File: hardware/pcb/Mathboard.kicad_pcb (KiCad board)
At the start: 2 copper layers, 95.6 x 74.3 mm, 44 parts, among them J1 TSW-112-06-T-S, J2 TSW-112-06-T-S, J4 Conn_01x07_Pin, SW1 SW_Push, SW10 SW_Push, SW11 SW_Push, SW12 SW_Push, SW13 SW_Push, SW14 SW_Push, SW15 SW_Push, SW16 SW_Push, SW17 PCM13SMTR, SW2 SW_Push, SW3 SW_Push, SW4 SW_Push, SW5 SW_Push, SW6 SW_Push, SW7 SW_Push, SW8 SW_Push, SW9 SW_Push

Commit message: Progress towards version 2
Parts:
- removed J1, J2: TSW-112-06-T-S, Connector_PinHeader_2.54mm:PinHeader_1x12_P2.54mm_Vertical
- removed J4: Conn_01x07_Pin, Connector_PinHeader_2.54mm:PinHeader_1x07_P2.54mm_Vertical
- removed REF**: OSHW-Logo_7.5x8mm_SilkScreen, Symbol:OSHW-Logo_7.5x8mm_SilkScreen
- removed REF**: KiCad-Logo_5mm_SilkScreen, Symbol:KiCad-Logo_5mm_SilkScreen
- removed REF**: WEEE-Logo_5.6x8mm_SilkScreen, Symbol:WEEE-Logo_5.6x8mm_SilkScreen
- added C10: 1u, Capacitor_SMD:C_0402_1005Metric, B.Cu at (100.5, 107.2)
- added C11: 1u, Capacitor_SMD:C_0402_1005Metric, B.Cu at (100.5, 106.0)
- added C12: 100n, Capacitor_SMD:C_0402_1005Metric, B.Cu at (110.8, 107.2)
- added C13: 100n, Capacitor_SMD:C_0402_1005Metric, B.Cu at (106.6, 101.8)
- added C14: 100n, Capacitor_SMD:C_0402_1005Metric, B.Cu at (100.5, 109.4)
- added C15: 100n, Capacitor_SMD:C_0402_1005Metric, B.Cu at (175.6, 47.7)
- added C16: 100n, Capacitor_SMD:C_0402_1005Metric, B.Cu at (102.5, 102.1)
- added C17: 100n, Capacitor_SMD:C_0402_1005Metric, B.Cu at (100.5, 110.3)
- added C18: 100n, Capacitor_SMD:C_0402_1005Metric, B.Cu at (110.6, 108.1)
- added C19: 100n, Capacitor_SMD:C_0402_1005Metric, B.Cu at (106.6, 112.0)
- added C2: 10u, Capacitor_SMD:C_0402_1005Metric, B.Cu at (128.2, 50.8)
- added C20: 100n, Capacitor_SMD:C_0402_1005Metric, B.Cu at (100.5, 108.5)
- added C3: 4.7u, Capacitor_SMD:C_0402_1005Metric, B.Cu at (108.7, 99.9)
- added C4: 10u, Capacitor_SMD:C_0402_1005Metric, B.Cu at (109.6, 99.9)
- added C5: 10u, Capacitor_SMD:C_0402_1005Metric, B.Cu at (124.1, 57.8)
- added C6: 10u, Capacitor_SMD:C_0402_1005Metric, B.Cu at (120.8, 55.2)
- added C7: 100n, Capacitor_SMD:C_0402_1005Metric, B.Cu at (93.4, 112.1)
- added C8: 15p, Capacitor_SMD:C_0402_1005Metric, B.Cu at (110.7, 105.0)
- added C9: 15p, Capacitor_SMD:C_0402_1005Metric, B.Cu at (115.0, 105.0)
- added D17: PMEG2010BELD, Diode_SMD:D_SOD-882D, B.Cu at (126.3, 54.2)
- added F1: 500mA, Fuse:Fuse_0603_1608Metric, B.Cu at (127.7, 52.8)
- added FB1: 600R, Resistor_SMD:R_0402_1005Metric, B.Cu at (129.6, 50.9)
- added J3: GT-USB-7010ASV, mathboard:USB_C_Receptacle_G-Switch_GT-USB-7010ASV, B.Cu at (124.7, 45.1)
- added Q1: 2N7002VC-, Package_TO_SOT_SMD:SOT-563, B.Cu at (116.7, 101.6)
- added Q2: 2N7002VC-, Package_TO_SOT_SMD:SOT-563, B.Cu at (104.8, 99.9)
- added R1: 10k, Resistor_SMD:R_0402_1005Metric, B.Cu at (117.6, 107.1)
- added R11: 10k, Resistor_SMD:R_0402_1005Metric, B.Cu at (93.4, 101.5)
- added R12: 27, Resistor_SMD:R_0402_1005Metric, B.Cu at (101.5, 112.0)
- added R13: 27, Resistor_SMD:R_0402_1005Metric, B.Cu at (102.5, 112.0)
- added R14: 1k, Resistor_SMD:R_0402_1005Metric, B.Cu at (113.2, 107.0)
- added R2: 10k, Resistor_SMD:R_0402_1005Metric, B.Cu at (102.4, 100.4)
- added R3: 10k, Resistor_SMD:R_0402_1005Metric, B.Cu at (116.7, 107.1)
- added R4: 51k, Resistor_SMD:R_0402_1005Metric, B.Cu at (106.7, 99.9)
- added R5: 51k, Resistor_SMD:R_0402_1005Metric, B.Cu at (107.7, 99.9)
- added R6: 51k, Resistor_SMD:R_0402_1005Metric, B.Cu at (108.2, 101.4)
- added R7: 5.1k, Resistor_SMD:R_0402_1005Metric, B.Cu at (121.9, 50.5)
- added R8: 5.1k, Resistor_SMD:R_0402_1005Metric, B.Cu at (126.3, 51.0)
- added R9: 1k, Resistor_SMD:R_0402_1005Metric, B.Cu at (99.4, 99.8)
- added SW18: SWITCH, mathboard:SW_Push_1P1T_XKB_TS-1187A, B.Cu at (121.0, 104.3)
- added U3: USBLC6-2P6, Package_TO_SOT_SMD:SOT-666, B.Cu at (121.3, 52.4)
- added U4: TLV74333PDBVR, Package_TO_SOT_SMD:SOT-23-5, B.Cu at (123.4, 55.7)
- added U5: W25Q128JVPIQ, Package_SO:SOIC-8W_5.3x5.3mm_P1.27mm, B.Cu at (95.8, 106.8)
- added U6: RP2040, Package_DFN_QFN:QFN-56-1EP_7x7mm_P0.4mm_EP3.2x3.2mm, B.Cu at (105.6, 106.8)
- added U7: 74LVC1T45, Package_TO_SOT_SMD:SOT-563, B.Cu at (175.3, 45.8)
- added Y1: 12MHz, Crystal:Crystal_SMD_2520-4Pin_2.5x2.0mm, B.Cu at (112.9, 105.0)
- moved U2 99.9 mm to (170.5, 45.8), turned to 0 degrees
- moved C1 93.5 mm to (166.2, 45.8), turned to -90 degrees
- moved D4 13.8 mm to (147.5, 51.4)
- moved D16 13.5 mm to (157.8, 105.5), turned to -90 degrees
- moved D15 13.4 mm to (129.2, 105.5), turned to -90 degrees
- moved D3 9.67 mm to (137.7, 51.4)
- moved SW17 9.40 mm to (139.7, 45.4)
- moved D5 6.58 mm to (167.0, 51.4), turned to -90 degrees
- moved H3 2.90 mm to (116.9, 112.3)
- moved D10 2.80 mm to (89.5, 83.5)
- moved D11 1.11 mm to (107.2, 86.5)
- moved D12 1.11 mm to (126.2, 86.5)
- moved D6 1.11 mm to (99.2, 67.5)
- moved D7 1.11 mm to (118.2, 67.5)
- moved D13 1.11 mm to (145.2, 86.5)
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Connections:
- net VDD renamed +5V
- SW17 pad 1: Net-(J2-Pin_11) -> /Microcontroller/7
- SW17 pad 2: Net-(J2-Pin_12) -> /Microcontroller/8
- SW17 pad 4: Net-(J4-Pin_1) -> /Microcontroller/9
- U2 pad 4: RGB_DIN -> /RGB_DIN
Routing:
- net GND: track 191.5 -> 39.7 mm, vias 1 -> 26
- net RGB_DIN: track 149.1 -> 0.00 mm, vias 2 -> 0
- net /Microcontroller/RGB_DO: track 0.00 -> 136.7 mm, vias 0 -> 2
- net /Microcontroller/USB-: track 0.00 -> 129.8 mm
- net /Microcontroller/USB+: track 0.00 -> 129.7 mm
- net +5V: track 173.4 -> 54.4 mm, vias 0 -> 2
- net /Microcontroller/9: track 0.00 -> 94.1 mm, vias 0 -> 2
- net /Microcontroller/8: track 0.00 -> 89.2 mm, vias 0 -> 2
- net /Microcontroller/7: track 0.00 -> 88.2 mm, vias 0 -> 2
- net ROW0: track 91.0 -> 147.3 mm, vias 0 -> 7
- net ROW1: track 65.5 -> 107.3 mm, vias 0 -> 6
- net COL2: track 65.0 -> 105.9 mm, vias 0 -> 2
- net COL4: track 95.5 -> 131.2 mm, vias 0 -> 2
- net Net-(J2-Pin_11): track 34.4 -> 0.00 mm
- net Net-(J2-Pin_12): track 30.3 -> 0.00 mm
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- added copper zone on B.Cu, net +3V3
- added copper zone on In1.Cu, net +3V3
- added copper zone on B.Cu, net +5V
- added copper zone on B.Cu, net /Microcontroller/RGB_DO
- added copper zone on B.Cu, net GND
- added copper zone on In2.Cu, net GND
- added copper zone on B.Cu, net Net-(J3-SHIELD)
- added copper zone on B.Cu, net VBUS
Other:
- copper layers 2 -> 4

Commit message: Version 2 sent to production
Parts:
- removed C9: 15p, Capacitor_SMD:C_0402_1005Metric
- removed FB1: 600R, Resistor_SMD:R_0402_1005Metric
- added C21: 4.7u, Capacitor_SMD:C_0402_1005Metric, B.Cu at (124.0, 56.3)
- added D18: A-SP192SGHC-C01-3C, mathboard:LED_SMD_0603_flat, B.Cu at (114.0, 43.2)
- added R10: 27, Resistor_SMD:R_0603_1608Metric, B.Cu at (105.9, 47.2)
- added R15: 27, Resistor_SMD:R_0603_1608Metric, B.Cu at (107.6, 47.2)
- added REF** (x2): OSHW-Logo_11.4x12mm_Copper, Symbol:OSHW-Logo_11.4x12mm_Copper, B.Cu at (148.6, 101.8)
- added REF** (x2): OSHW-Logo2_9.8x8mm_Copper, Symbol:OSHW-Logo2_9.8x8mm_Copper, B.Cu at (148.6, 112.3)
- added RV1: 20k, Potentiometer_SMD:Potentiometer_Bourns_TC33X_Vertical, B.Cu at (102.3, 47.6)
- added TP1: TestPoint, TestPoint:TestPoint_Pad_2.0x2.0mm, B.Cu at (88.2, 46.1)
- added TP2: TestPoint, TestPoint:TestPoint_Pad_2.0x2.0mm, B.Cu at (88.2, 49.1)
- added U1: W25Q64JV, Package_SON:WSON-8-1EP_8x6mm_P1.27mm_EP3.4x4.3mm, B.Cu at (95.8, 106.8)
- C2, C4, C5: value 10u -> 4.7u
- C6: value 10u -> 30p; footprint Capacitor_SMD:C_0402_1005Metric -> Capacitor_SMD:C_0603_1608Metric
- C8: value 15p -> 30p; footprint Capacitor_SMD:C_0402_1005Metric -> Capacitor_SMD:C_0603_1608Metric
- D17: value PMEG2010BELD -> DSL14; footprint Diode_SMD:D_SOD-882D -> Diode_SMD:D_SOD-123
- J3: value GT-USB-7010ASV -> TYPE-C sinking plate; footprint mathboard:USB_C_Receptacle_G-Switch_GT-USB-7010ASV -> mathboard:USB_C_Receptacle_XYECONN TYPE-C-F02C-1BBWC1.6
- R12, R13: footprint Resistor_SMD:R_0402_1005Metric -> Resistor_SMD:R_0603_1608Metric
- SW17: value PCM13SMTR -> MSK13C02; footprint mathboard:SWITCH_3SMTR -> mathboard:SWITCH_MSK13C02
- U2: footprint LED_SMD:SK6812-MINI-E -> mathboard:SK6812-MINI-E
- U4: value TLV74333PDBVR -> XC6206P332MR-G; footprint Package_TO_SOT_SMD:SOT-23-5 -> Package_TO_SOT_SMD:SOT-23
- U5: value W25Q128JVPIQ -> PSSI2021SAY; footprint Package_SO:SOIC-8W_5.3x5.3mm_P1.27mm -> Package_TO_SOT_SMD:SOT-353_SC-70-5
- moved U5 62.9 mm to (110.1, 45.5), turned to 180 degrees
- moved C6 50.1 mm to (115.3, 105.0)
- moved D3 12.9 mm to (128.1, 60.0), turned to 90 degrees
- moved D2 11.8 mm to (109.9, 60.3), turned to 90 degrees
- moved D1 10.6 mm to (93.9, 58.7), turned to 90 degrees
- moved D5 8.80 mm to (166.9, 60.2), turned to 90 degrees
- moved D4 8.71 mm to (147.8, 60.1), turned to 90 degrees
- moved C5 5.34 mm to (119.3, 55.5), turned to -90 degrees
- moved SW17 3.04 mm to (142.6, 44.5)
- moved SW18 2.41 mm to (122.8, 105.9)
- moved Q1 2.41 mm to (118.5, 103.2)
- moved C11 2.40 mm to (100.5, 108.4)
- moved C20 2.30 mm to (100.5, 106.2)
- moved C10 2.20 mm to (100.5, 109.4)
- moved C14 2.20 mm to (100.5, 107.2)
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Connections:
- C2 pad 1: VBUS -> GND
- C2 pad 2: GND -> VBUS
- C5 pad 1: +5V -> +3V3
- C6 pad 1: +3V3 -> GND
- C6 pad 2: GND -> Net-(C6-Pad2)
- J3 pad S1: Net-(J3-SHIELD) -> GND
- R14 pad 1: Net-(C9-Pad2) -> Net-(C6-Pad2)
- U4 pad 1: +5V -> GND
- U4 pad 2: GND -> +3V3
- U5 pad 1: /Microcontroller/QSPI_CS -> unconnected-(U5-NC-Pad1)
- U5 pad 2: /Microcontroller/QSPI_SD1 -> Net-(D18-K)
- U5 pad 3: /Microcontroller/QSPI_SD2 -> GND
- U5 pad 4: GND -> Net-(R10-Pad1)
- U5 pad 5: /Microcontroller/QSPI_SD0 -> +5V
- Y1 pad 1: Net-(C9-Pad2) -> Net-(C6-Pad2)
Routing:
- net +5V: track 54.4 -> 93.5 mm, vias 2 -> 4
- net Net-(D18-A): track 0.00 -> 29.3 mm, vias 0 -> 2
- net ROW0: track 147.3 -> 125.4 mm
- net /Microcontroller/USB-: track 129.8 -> 113.3 mm
- net /Microcontroller/USB+: track 129.7 -> 113.4 mm
- net VBUS: track 3.45 -> 12.0 mm, vias 0 -> 2
- net GND: track 39.7 -> 47.1 mm, vias 26 -> 33
- net Net-(D3-A): track 9.90 -> 2.98 mm
- net COL0: track 73.8 -> 80.5 mm
- net COL1: track 61.1 -> 65.2 mm
- net Net-(R10-Pad2): track 0.00 -> 4.03 mm
- net Net-(Q1A-D): track 18.1 -> 21.9 mm, vias 0 -> 2
- net Net-(D18-K): track 0.00 -> 3.40 mm
- net Net-(R10-Pad1): track 0.00 -> 3.34 mm
- net Net-(C6-Pad2): track 0.00 -> 2.88 mm
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- removed copper zone on B.Cu, net /Microcontroller/RGB_DO
- removed copper zone on B.Cu, net Net-(J3-SHIELD)
- removed copper zone on B.Cu, net VBUS
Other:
- board size 95.6 x 74.3 mm -> 95.6 x 73.6 mm
- board text added: "GND"
- board text added: "LED"
- board text added: "MATHBOARD V1.0 PCB REV 3 MAGNE EIK LAURITZEN"
- board text removed: "MATHBOARD V1.0 PCB REV 2 MAGNE EIK LAURITZEN"

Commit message: Revision 4
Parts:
- removed H1, H2, H3: MountingHole, MountingHole:MountingHole_2.7mm
- removed the REF** at (148.6, 112.3) (x2)
- removed RV1: 20k, Potentiometer_SMD:Potentiometer_Bourns_TC33X_Vertical
- removed TP1, TP2: TestPoint, TestPoint:TestPoint_Pad_2.0x2.0mm
- added REF**: WEEE-Logo_5.6x8mm_SilkScreen, Symbol:WEEE-Logo_5.6x8mm_SilkScreen, F.Cu at (88.9, 71.3)
- added REF**: ESD-Logo_6.6x6mm_SilkScreen, Symbol:ESD-Logo_6.6x6mm_SilkScreen, F.Cu at (88.6, 80.6)
- added REF**: KiCad-Logo_5mm_SilkScreen, Symbol:KiCad-Logo_5mm_SilkScreen, F.Cu at (170.8, 81.5)
- C1, C10, C11, C12, C13, C14, C15, C16, C17, C18, C19, C2, C20, C21, C3, C4, C5, C6, C7, C8, D1, D10, D11, D12, D13, D14, D15, D16, D17, D18, D2, D3, D4, D5, D6, D7, D8, D9, F1, J3, Q1, Q2, R1, R11, R12, R13, R14, R2, R3, R4, R5, R6, R7, R8, R9, REF** (x2), SW17, SW18, U2, U3, U4, U5, U6, U7, Y1: moved to F.Cu
- R10, R15: value 27 -> 10k; footprint Resistor_SMD:R_0603_1608Metric -> Resistor_SMD:R_0402_1005Metric; moved to F.Cu
- SW1, SW10, SW11, SW12, SW13, SW14, SW15, SW16, SW2, SW3, SW4, SW5, SW6, SW7, SW8, SW9: moved to B.Cu
- U1: footprint Package_SON:WSON-8-1EP_8x6mm_P1.27mm_EP3.4x4.3mm -> mathboard:WSON-8-1EP_8x6mm_P1.27mm_EP3.4x4.3mm; moved to F.Cu
- moved C15 87.4 mm to (88.0, 50.5), turned to 0 degrees
- moved D10 87.3 mm to (175.7, 97.9), turned to 90 degrees
- moved U7 86.8 mm to (88.3, 48.6)
- moved SW10 79.0 mm to (171.3, 89.0), turned to 180 degrees
- moved SW5 79.0 mm to (92.3, 51.0), turned to 180 degrees
- moved D1 78.8 mm to (172.7, 59.8)
- moved R11 76.8 mm to (170.2, 101.9), turned to 180 degrees
- moved C7 75.8 mm to (169.2, 111.7)
- moved U2 75.4 mm to (94.1, 45.4), turned to 180 degrees
- moved SW1 73.0 mm to (168.3, 51.0), turned to 180 degrees
- moved SW14 73.0 mm to (95.3, 89.0), turned to 180 degrees
- moved U1 71.9 mm to (167.8, 106.8)
- moved D5 70.2 mm to (96.7, 60.2)
- moved C1 66.8 mm to (98.4, 45.4)
- moved SW16 66.5 mm to (97.0, 108.0), turned to 180 degrees
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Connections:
- D18 pad 2: Net-(D18-A) -> GND
- R10 pad 1: Net-(R10-Pad1) -> +3V3
- R15 pad 1: Net-(R10-Pad1) -> Net-(R10-Pad2)
- R15 pad 2: Net-(R10-Pad2) -> Net-(R15-Pad2)
- U5 pad 4: Net-(R10-Pad1) -> Net-(R15-Pad2)
- U5 pad 5: +5V -> +3V3
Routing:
- net Net-(D18-A): track 29.3 -> 0.00 mm, vias 2 -> 0
- net /Microcontroller/USB+: track 113.4 -> 95.0 mm
- net /Microcontroller/USB-: track 113.3 -> 95.2 mm
- net +5V: track 93.5 -> 77.0 mm, vias 4 -> 3
- net +1V1: track 4.29 -> 14.7 mm
- net ROW2: track 98.1 -> 108.3 mm
- net COL0: track 80.5 -> 71.7 mm
- net Net-(D10-A): track 10.2 -> 2.55 mm
- net +3V3: track 22.9 -> 17.7 mm, vias 13 -> 14
- net ROW3: track 61.0 -> 66.0 mm
- net ROW0: track 125.4 -> 129.6 mm
- net Net-(R10-Pad1): track 3.34 -> 0.00 mm
- net Net-(R10-Pad2): track 4.03 -> 1.00 mm
- net Net-(D16-A): track 6.13 -> 3.17 mm
- net Net-(D15-A): track 6.13 -> 3.28 mm
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- added copper zone on F.Cu, net +3V3
- added copper zone on In2.Cu, net +3V3
- added copper zone on F.Cu, net GND
- added copper zone on In1.Cu, net GND
- removed copper zone on B.Cu, net +3V3
- removed copper zone on In1.Cu, net +3V3
- removed copper zone on B.Cu, net +5V
- removed copper zone on B.Cu, net GND
- removed copper zone on In2.Cu, net GND
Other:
- outline, holes or cut-outs redrawn
- board text added: "MATHBOARD V1.4 @MAGNE LAURITZEN"
- board text removed: "GND"
- board text removed: "LED"
- board text removed: "MATHBOARD V1.0 PCB REV 3 MAGNE EIK LAURITZEN"

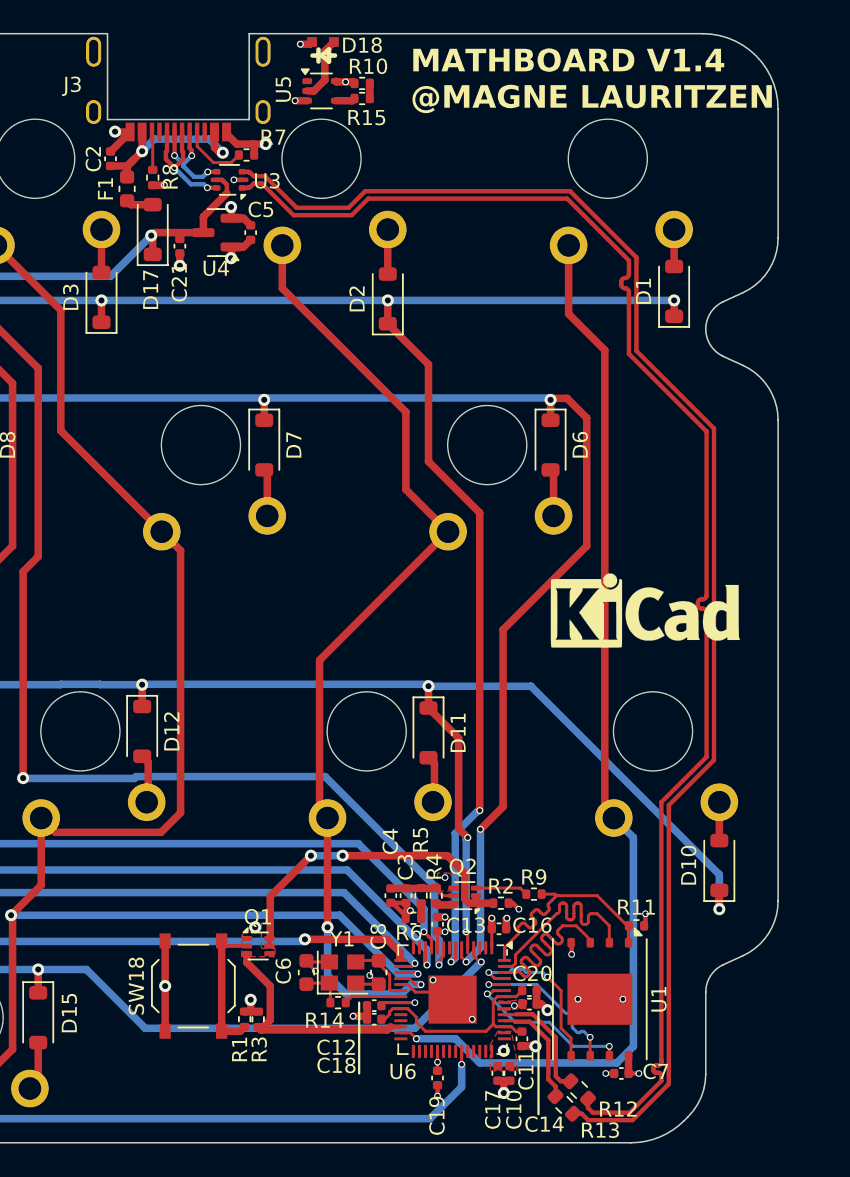
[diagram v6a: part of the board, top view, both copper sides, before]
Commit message: Added version encoder resistors
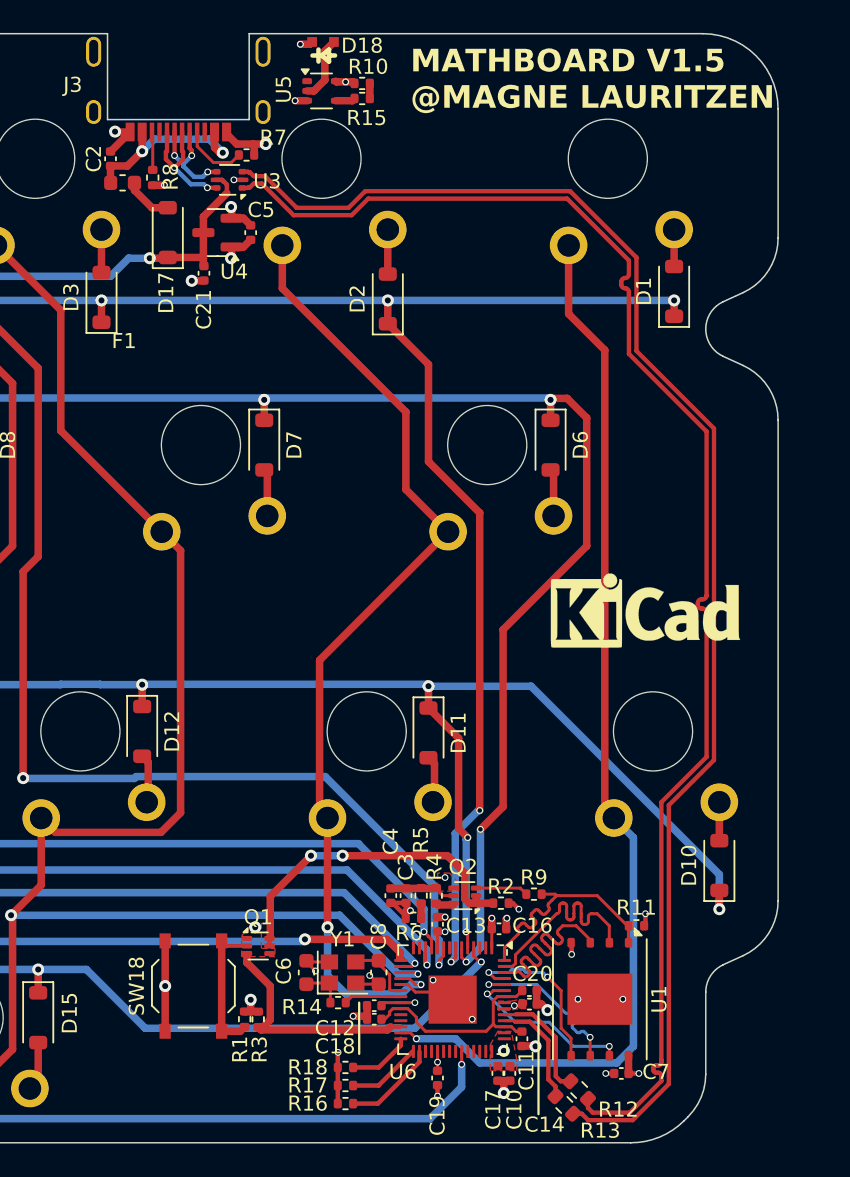
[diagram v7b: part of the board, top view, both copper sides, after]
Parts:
- added R16: 1k, Resistor_SMD:R_0402_1005Metric, F.Cu at (150.9, 113.7)
- added R17: 1k, Resistor_SMD:R_0402_1005Metric, F.Cu at (150.9, 112.5)
- added R18: 1k, Resistor_SMD:R_0402_1005Metric, F.Cu at (150.9, 111.3)
- moved C21 2.41 mm to (141.5, 58.6)
- moved D17 1.02 mm to (139.1, 55.9)
- moved F1 0.50 mm to (136.1, 52.6), turned to 0 degrees
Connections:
- U6 pad 28: /Microcontroller/LED -> /Microcontroller/17
- U6 pad 29: unconnected-(U6-GPIO18-Pad29) -> /Microcontroller/18
- U6 pad 30: unconnected-(U6-GPIO19-Pad30) -> /Microcontroller/19
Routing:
- net /Microcontroller/19: track 0.00 -> 6.25 mm
- net /Microcontroller/18: track 0.00 -> 4.89 mm
- net /Microcontroller/17: track 0.00 -> 4.21 mm
- net GND: track 45.8 -> 49.2 mm, vias 31 -> 32
- net Net-(D17-A): track 1.81 -> 3.18 mm
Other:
- board text added: "MATHBOARD V1.5 @MAGNE LAURITZEN"
- board text removed: "MATHBOARD V1.4 @MAGNE LAURITZEN"
